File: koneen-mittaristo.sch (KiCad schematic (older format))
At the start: 21 parts, among them J1 30A, J2 J1, J4 J2

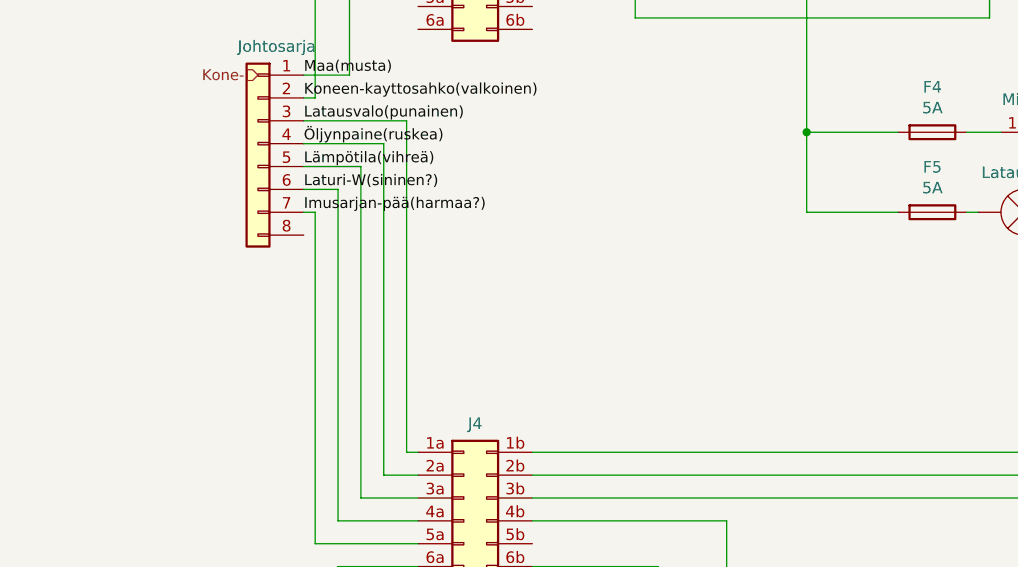
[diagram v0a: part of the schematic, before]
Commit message: IDitä muutettu osoitteistusluonnoksen mukaan
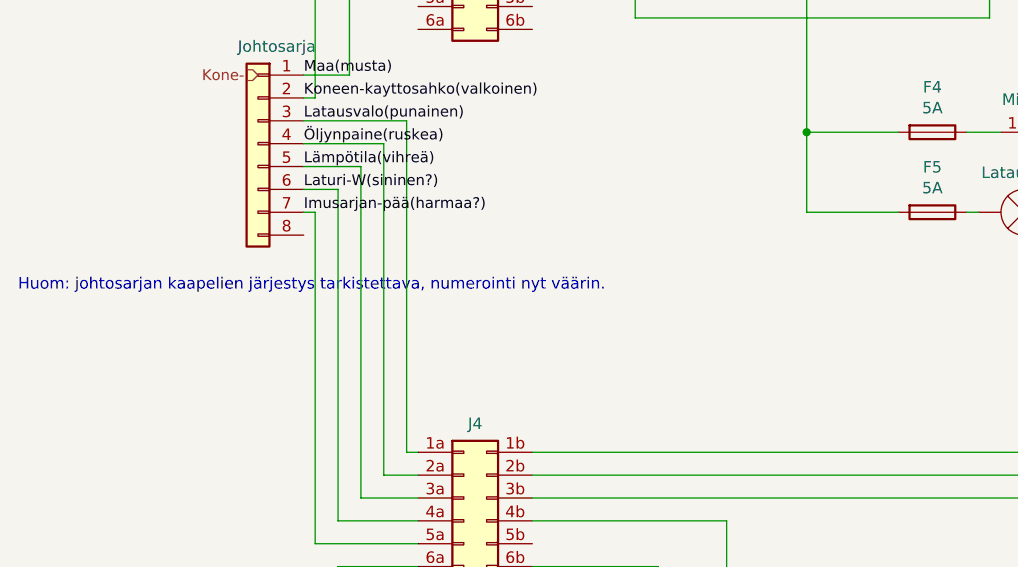
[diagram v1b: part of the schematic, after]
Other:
- note added: "Huom: johtosarjan kaapelien järjestys tarkistettava, numerointi nyt väärin."
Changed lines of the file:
@@
 encoding utf-8
 Sheet 4 4
-Title "Särkänlinnan mottorin mittariston kytkentä"
+Title "Särkänlinnan moottorin mittariston kytkentä"
 Date "2019-12-02-Draft"
 Rev "0"
@@
 Wire Wire Line
 	2050 3800 2500 3800
+Text Notes 750  2700 0    50   ~ 0
+Huom: johtosarjan kaapelien järjestys tarkistettava, numerointi nyt väärin.
 $EndSCHEMATC

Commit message: Koneen sähköpiirros järjestetty uudelleen
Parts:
- removed Jännitemittari, Kierroslukumittari, Lämpömittari, Polttoainemittari, Tuntimittari, Öljynpainemittari: Koneen-mittari-1-mittausnapa, symbol SL-sahkot-rescue:Koneen-mittari-1-mittausnapa-Connector_Generic
- added J3: J3 - Maa, symbol Connector_Generic:Conn_02x08_Row_Letter_Last
- added Jännitemittari, Käyttötuntimittari: Koneen-mittari-4-nap-ei-mittausta, symbol SL-sahkot-rescue:Koneen-mittari-4-nap-ei-mittausta
- added Kierroslukumittari, Polttoainemittari: Koneen-mittari-4-nap, symbol SL-sahkot-rescue:Koneen-mittari-4-nap
- added Lämpömittari, Öljynpainemittari: Koneen-mittari-5-nap, symbol SL-sahkot-rescue:Koneen-mittari-5-nap
- F3: value 15A ? -> 5A
- F4: value 5A -> 15A ?
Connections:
- net Mittari+: now reaches J2.2b (Pin_2b)
- net Mittari+: now also Jännitemittari.+ (Pin_3), Kierroslukumittari.+ (Pin_3), Käyttötuntimittari.+ (Pin_3), Lämpömittari.+ (Pin_3), Polttoainemittari.+ (Pin_3), Öljynpainemittari.+ (Pin_3)
- net Mittarivalo+: now reaches J2.7b (Pin_7b)
- net Mittarivalo+: now also Jännitemittari.+Lamp (Pin_1), Kierroslukumittari.+Lamp (Pin_1), Käyttötuntimittari.+Lamp (Pin_1), Lämpömittari.+Lamp (Pin_1), Polttoainemittari.+Lamp (Pin_1), Öljynpainemittari.+Lamp (Pin_1)
- net at J4.2b (Pin_2b): now also Latausvalo.2 (+)
- net at J4.1b (Pin_1b): now also Kierroslukumittari.Mittaus (Pin_5); no longer Latausvalo.2 (+)
- net at J4.3b (Pin_3b): now also Lämpömittari.Mittaus (Pin_5)
- net at J4.4b (Pin_4b): now also Öljynpainemittari.Mittaus (Pin_5)
- net at J4.6a (Pin_6a): no longer Polttoaineanturi.1 (Pin_1)
- net at J4.7a (Pin_7a): now also Polttoaineanturi.1 (Pin_1); no longer Polttoaineanturi.2 (Pin_2)
- net at J4.8a (Pin_8a): now also Polttoaineanturi.2 (Pin_2)
- net Maa: now reaches J4.8b (Pin_8b)
- net Maa: now also J1.3b (Pin_3b), J3.1b (Pin_1b), Jännitemittari.- (Pin_4), Jännitemittari.-Lamp (Pin_5), Kierroslukumittari.- (Pin_4), Käyttötuntimittari.- (Pin_4), Käyttötuntimittari.-Lamp (Pin_5), Lämpömittari.- (Pin_4), Lämpömittari.-Lamp (Pin_2), Polttoainemittari.- (Pin_4), Öljynpainemittari.- (Pin_4), Öljynpainemittari.-Lamp (Pin_2)
- net at Mittarivalot.1 (A): now also F3.1; no longer F4.1
- net Gnd: no longer names the net of J4.7b (Pin_7b)
- net Gnd: now also Polttoainemittari.Mittaus (Pin_5); no longer J1.4b (Pin_4b)
- net Imusarjan-pää(harmaa?): no longer names the net of J4.5a (Pin_5a)
- net Imusarjan-pää(harmaa?): no longer Johtosarja.7 (Pin_7)
- net Koneen-kayttosahko(valkoinen): no longer names the net of Johtosarja.2 (Pin_2)
- net Koneen-kayttosahko(valkoinen): now also J4.2a (Pin_2a); no longer J1.3a (Pin_3a)
- net Latausvalo(punainen): no longer names the net of J4.1a (Pin_1a)
- net Latausvalo(punainen): now also Johtosarja.1 (Pin_1); no longer Johtosarja.3 (Pin_3)
- net Laturi-W(sininen?): no longer names the net of J4.4a (Pin_4a)
- net Laturi-W(sininen?): now also Johtosarja.4 (Pin_4); no longer Johtosarja.6 (Pin_6)
- net Lämpötila(vihreä): no longer names the net of J4.3a (Pin_3a)
- net Lämpötila(vihreä): now also Johtosarja.3 (Pin_3); no longer Johtosarja.5 (Pin_5)
- net Maa(musta): no longer names the net of J1.4a (Pin_4a)
- net Maa(musta): now also Johtosarja.7 (Pin_7); no longer Johtosarja.1 (Pin_1)
- removed net Öljynpaine(ruskea): J4.2a (Pin_2a), Johtosarja.4 (Pin_4)
- new net: J1.3a (Pin_3a), Johtosarja.6 (Pin_6)
- new net: F4.1, J1.4b (Pin_4b)
- new net: J3.1a (Pin_1a), J3.2a (Pin_2a), J3.3a (Pin_3a), J3.4a (Pin_4a), J3.5a (Pin_5a), J3.6a (Pin_6a), J3.7a (Pin_7a), J3.8a (Pin_8a)
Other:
- note added: "Kierroslukumittari (W) (sininen)"
- note added: "Koneen käyttösähkö (valkoinen)"
- note added: "Koneen runko; maa (musta)"
- note added: "Latausvalo (punainen)"
- note added: "Lämpöanturi (vihreä)"
- note added: "Sulakkeet"
- note added: "Thermostart (harmaa)"
- note added: "Öljynpaineanturi (ruskea)"
- note removed: "Huom: johtosarjan kaapelien järjestys tarkistettava, numerointi nyt väärin."
- moved on the sheet: F1, F2, F3, F4, F5, J1, J2, J4, JS_pun, JS_sin, Johtosarja, Latausvalo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

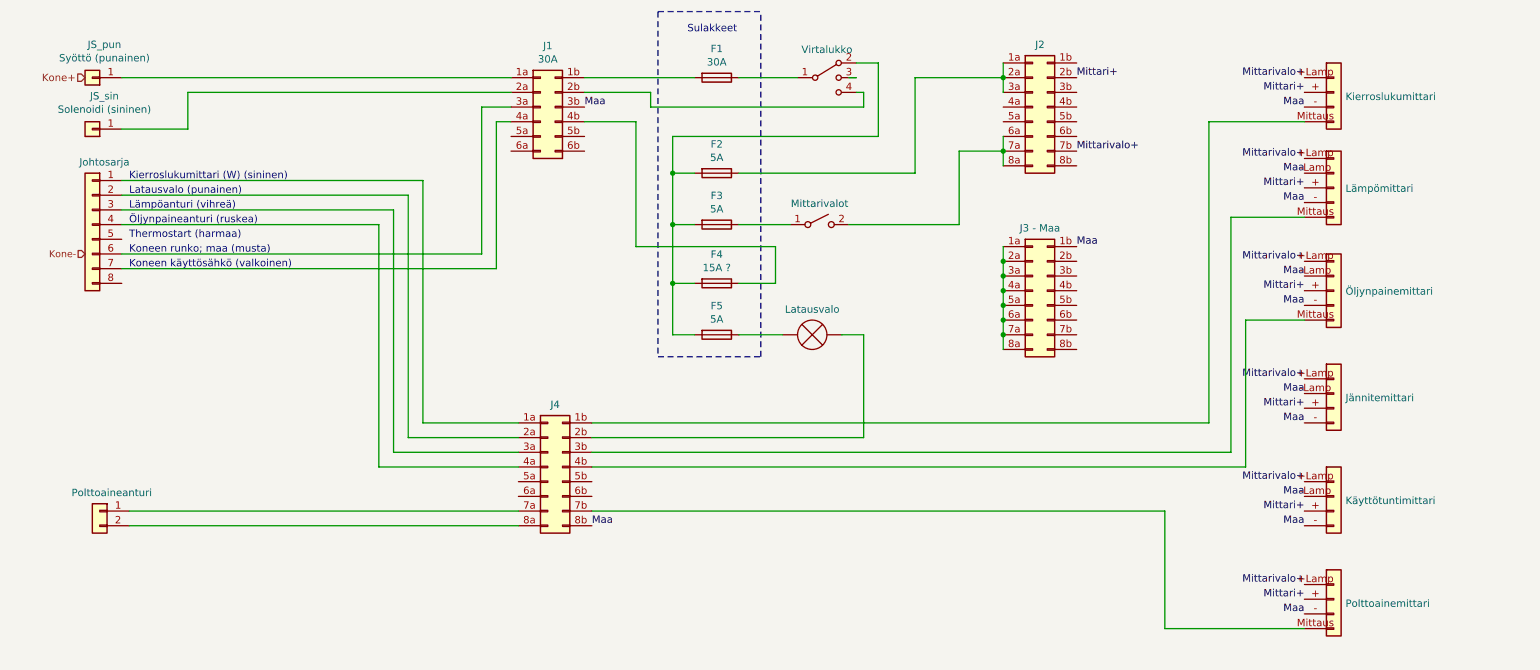
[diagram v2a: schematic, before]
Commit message: Koneen kytkentää päivitetty toteutuneen johdotuksen mukaiseksi;
 * johtojen merkinnät puuttuvat
 * mittareiden kytkennät kytkentärimojen
   napoihin puuttuvat
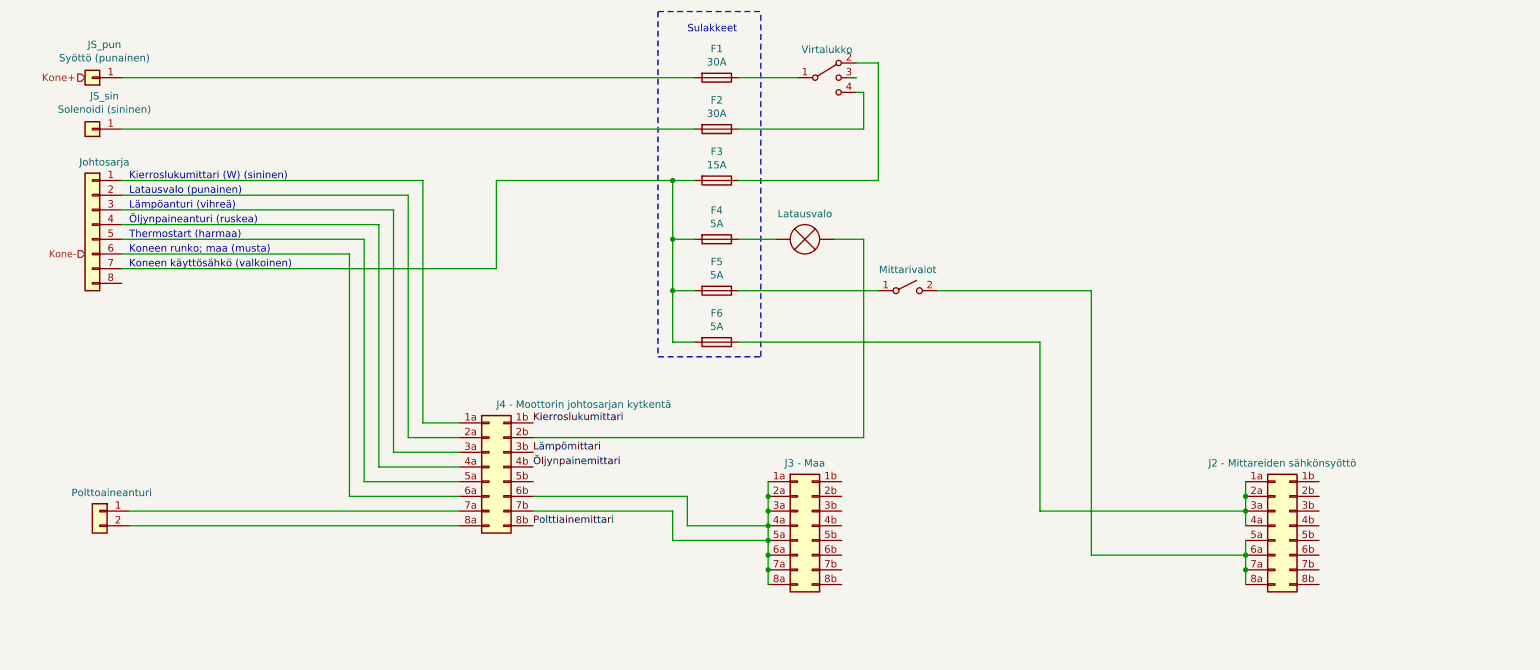
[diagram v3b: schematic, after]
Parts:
- removed J1: 30A, symbol Connector_Generic:Conn_02x06_Row_Letter_Last
- removed Jännitemittari, Käyttötuntimittari: Koneen-mittari-4-nap-ei-mittausta, symbol SL-sahkot-rescue:Koneen-mittari-4-nap-ei-mittausta
- removed Kierroslukumittari, Polttoainemittari: Koneen-mittari-4-nap, symbol SL-sahkot-rescue:Koneen-mittari-4-nap
- removed Lämpömittari, Öljynpainemittari: Koneen-mittari-5-nap, symbol SL-sahkot-rescue:Koneen-mittari-5-nap
- added F6: 5A, symbol Device:Fuse
- F2: value 5A -> 30A
- F3: value 5A -> 15A
- F4: value 15A ? -> 5A
- J2: value J1 -> J2 - Mittareiden sähkönsyöttö
- J4: value J2 -> J4 - Moottorin johtosarjan kytkentä
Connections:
- net at J2.1a (Pin_1a), J2.2a (Pin_2a), J2.3a (Pin_3a): now also J2.4a (Pin_4a), F6.1; no longer F2.1
- net at J2.5a (Pin_5a): now also J2.6a (Pin_6a), J2.7a (Pin_7a), J2.8a (Pin_8a), Mittarivalot.2 (B)
- net Kierroslukumittari: now reaches J4.1b (Pin_1b)
- net Lämpömittari: now reaches J4.3b (Pin_3b)
- net Öljynpainemittari: now reaches J4.4b (Pin_4b)
- net at J4.5a (Pin_5a): now also Johtosarja.5 (Pin_5)
- net at J4.6a (Pin_6a): now also Johtosarja.6 (Pin_6)
- net at J4.6b (Pin_6b): now also J3.1a (Pin_1a), J3.2a (Pin_2a), J3.3a (Pin_3a), J3.4a (Pin_4a), J3.5a (Pin_5a), J3.6a (Pin_6a), J3.7a (Pin_7a), J3.8a (Pin_8a), J4.7b (Pin_7b)
- net at Mittarivalot.1 (A): now also F5.1; no longer F3.1
- net at F1.2: now also JS_pun.1 (Pin_1)
- net at JS_sin.1 (Pin_1): now also F2.2
- net at Virtalukko.4: now also F2.1
- net at Johtosarja.7 (Pin_7): now also F3.2, F4.2, F5.2, F6.2
- net at F4.1: now also Latausvalo.1 (-)
- net Maa: no longer names the net of J3.1b (Pin_1b)
- net Maa: no longer J4.8b (Pin_8b)
- net Mittari+: no longer names the net of J2.2b (Pin_2b)
- net Mittarivalo+: no longer names the net of J2.7b (Pin_7b)
- new net: F3.1, Virtalukko.2
- new net Polttiainemittari: J4.8b (Pin_8b)
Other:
- moved on the sheet: F2, F3, F4, F5, Latausvalo, Mittarivalot
